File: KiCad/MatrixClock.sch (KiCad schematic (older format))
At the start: 36 parts, among them J1 FDTI 3.3V, J2 USB_OTG, J3 CONN_01X05, J4 CONN_01X05, J5 DISP_PWR, M1 Module_MAX7219, M2 Module_MAX7219, M3 Module_MAX7219, M4 Module_MAX7219, M5 Module_MAX7219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

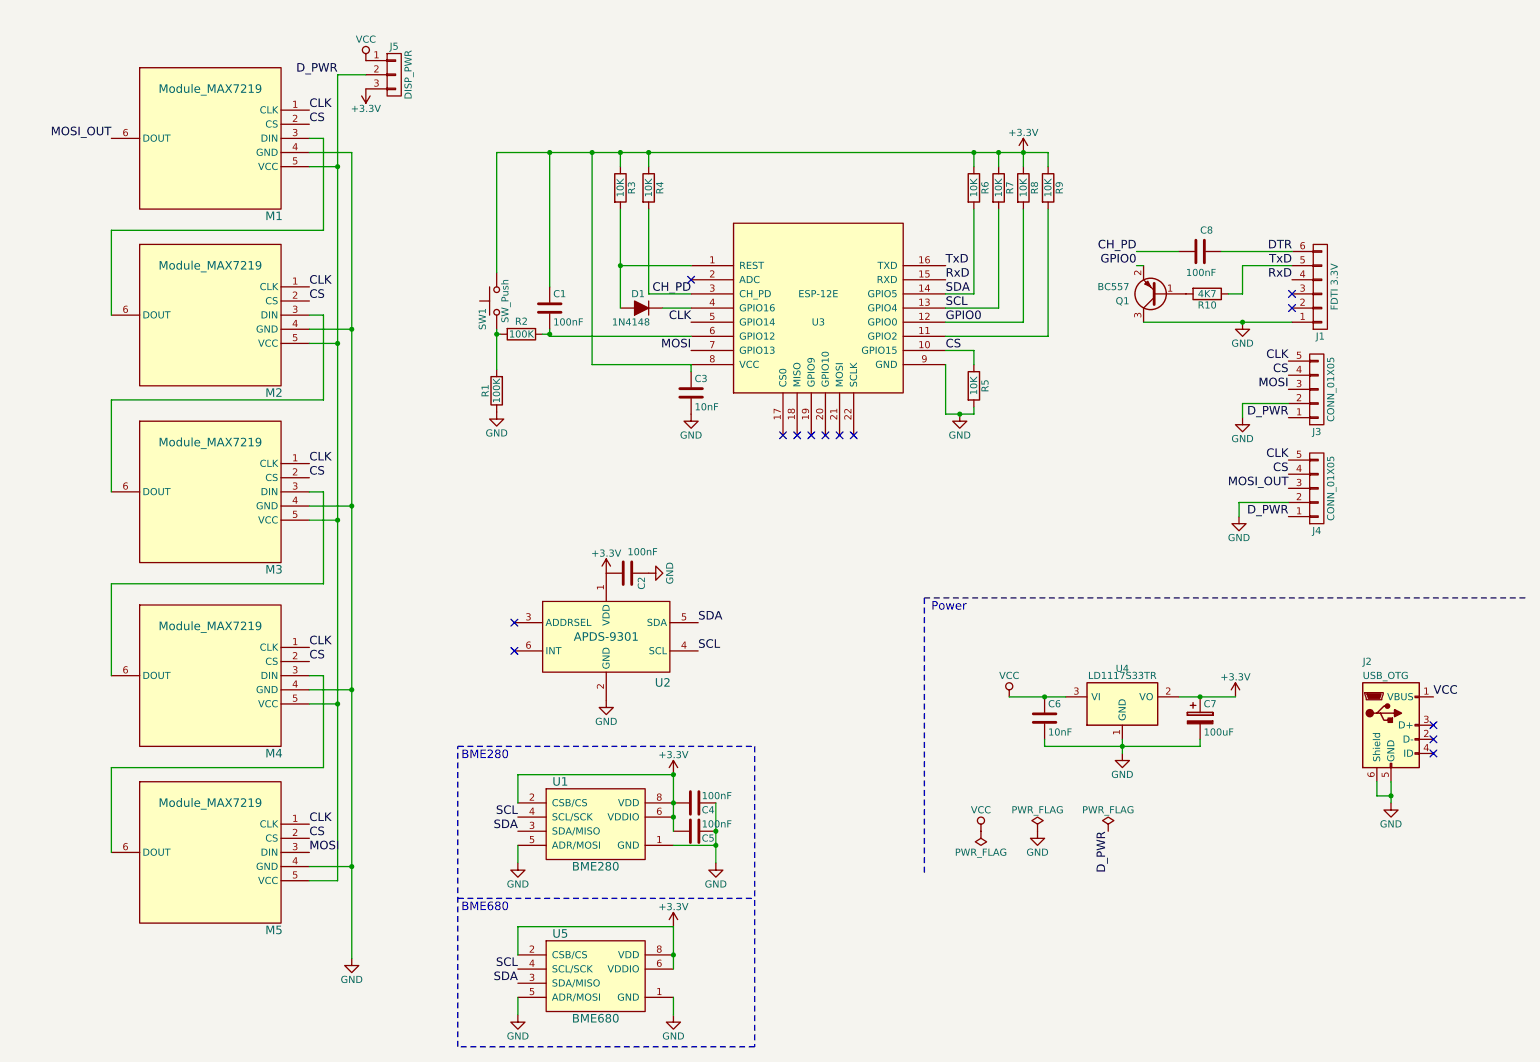
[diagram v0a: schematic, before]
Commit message: Bumped version to 0.5
Features:
* Reworked the matrix module layout, the 2 header pins where 0.4mm off.
* Added BH1750FVI as an alternative light sensor.

Fixed issues:
* R10 should be connected to RX, not TX (seen from ESP12, not FTDI connector)
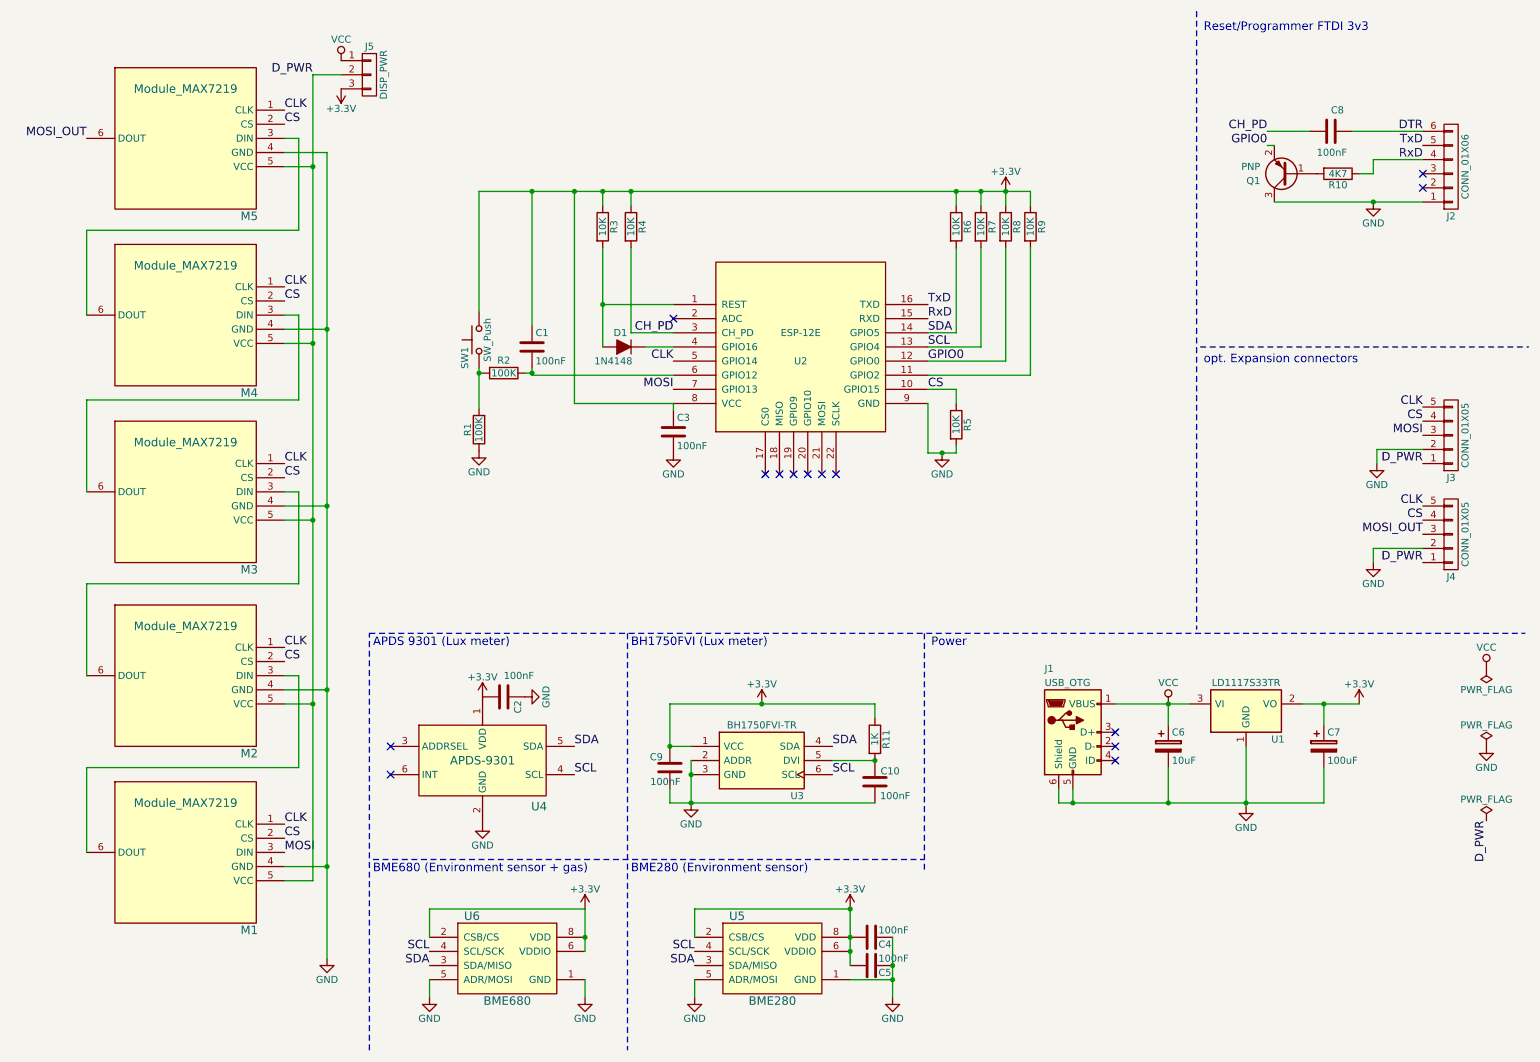
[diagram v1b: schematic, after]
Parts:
- removed C6: 10nF, Capacitors_SMD:C_0805, symbol C
- added C10, C2: 100nF, Capacitors_SMD:C_0805, symbol C
- added C6: 10uF, Capacitors_SMD:CP_Elec_3x5.3, symbol CP
- added R11: 1K, Resistors_SMD:R_0805_HandSoldering, symbol R
- added U3: BH1750FVI-TR, Private:WSOF6, symbol BH1750FVI-TR
- C1, C4, C5, C8: MPN (none) -> C0805C104K5RACTU
- C3: value 10nF -> 100nF; MPN (none) -> C0805C104K5RACTU
- C7: MPN ? -> UWT1C101MCL1GB
- C9: renamed from C2; MPN (none) -> C0805C104K5RACTU
- D1: MPN (none) -> 1N4148W-TP
- J2: renamed from J1; value FDTI 3.3V -> CONN_01X06; MPN (none) -> P125-1106A1BS116A1
- J3, J4: MPN ? -> P125-1106A1BS116A1
- J5: MPN ? -> (none)
- M1: renamed from M5; MPN (none) -> Red_MAX7219_8x8_dot_matrix
- M2: renamed from M4; MPN (none) -> Red_MAX7219_8x8_dot_matrix
- M3: MPN (none) -> Red_MAX7219_8x8_dot_matrix
- M4: renamed from M2; MPN ? -> Red_MAX7219_8x8_dot_matrix
- M5: renamed from M1; MPN ? -> Red_MAX7219_8x8_dot_matrix
- Q1: value BC557 -> PNP; MPN ? -> MMSS8550-H-TP
- R1, R2: MPN (none) -> RC0805JR-07100KL
- R10: MPN (none) -> RC0805JR-074K7L
- R3, R4, R5, R6, R7, R8, R9: MPN (none) -> RC0805JR-0710KL
- U1: renamed from U4; footprint TO_SOT_Packages_SMD:SOT-223 -> TO_SOT_Packages_SMD:SOT-223-3Lead_TabPin2; MPN (none) -> LD1117AS33TR
- U2: renamed from U3; MPN (none) -> ESP-12E
- U4: renamed from U2; MPN (none) -> APDS-9301-020
- U5: renamed from U1; MPN ? -> BME280
- U6: renamed from U5; MPN ? -> BME680
- renumbered J2 to J1
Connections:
- net +3V3: now also C2.2, R11.1, U3.1 (VCC)
- net GND: now also C10.1, C2.1, C6.2, U3.2 (ADDR), U3.3 (GND)
- net RxD: now also R10.1
- net SCL: now also U3.6 (SCL)
- net SDA: now also U3.4 (SDA)
- net TxD: no longer R10.1
- net VCC: now also C6.1
- new net: C10.2, R11.2, U3.5 (DVI)
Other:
- note added: "APDS 9301 (Lux meter)"
- note added: "BH1750FVI (Lux meter)"
- note added: "BME280 (Environment sensor)"
- note added: "BME680 (Environment sensor + gas)"
- note added: "Reset/Programmer FTDI 3v3"
- note added: "opt. Expansion connectors"
- note removed: "BME280"
- note removed: "BME680"
- moved on the sheet: C1, C3, C4, C5, C7, C8, C9, D1, J1, J2, J3, J4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
